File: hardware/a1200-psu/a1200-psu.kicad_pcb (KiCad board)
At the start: 2 copper layers, 147 x 76 mm, 61 parts, among them J1 220V, J2 Conn_01x05, Q1 P2N60, U1 UC3844_DIP8, U2 PC817, U3 TL431D

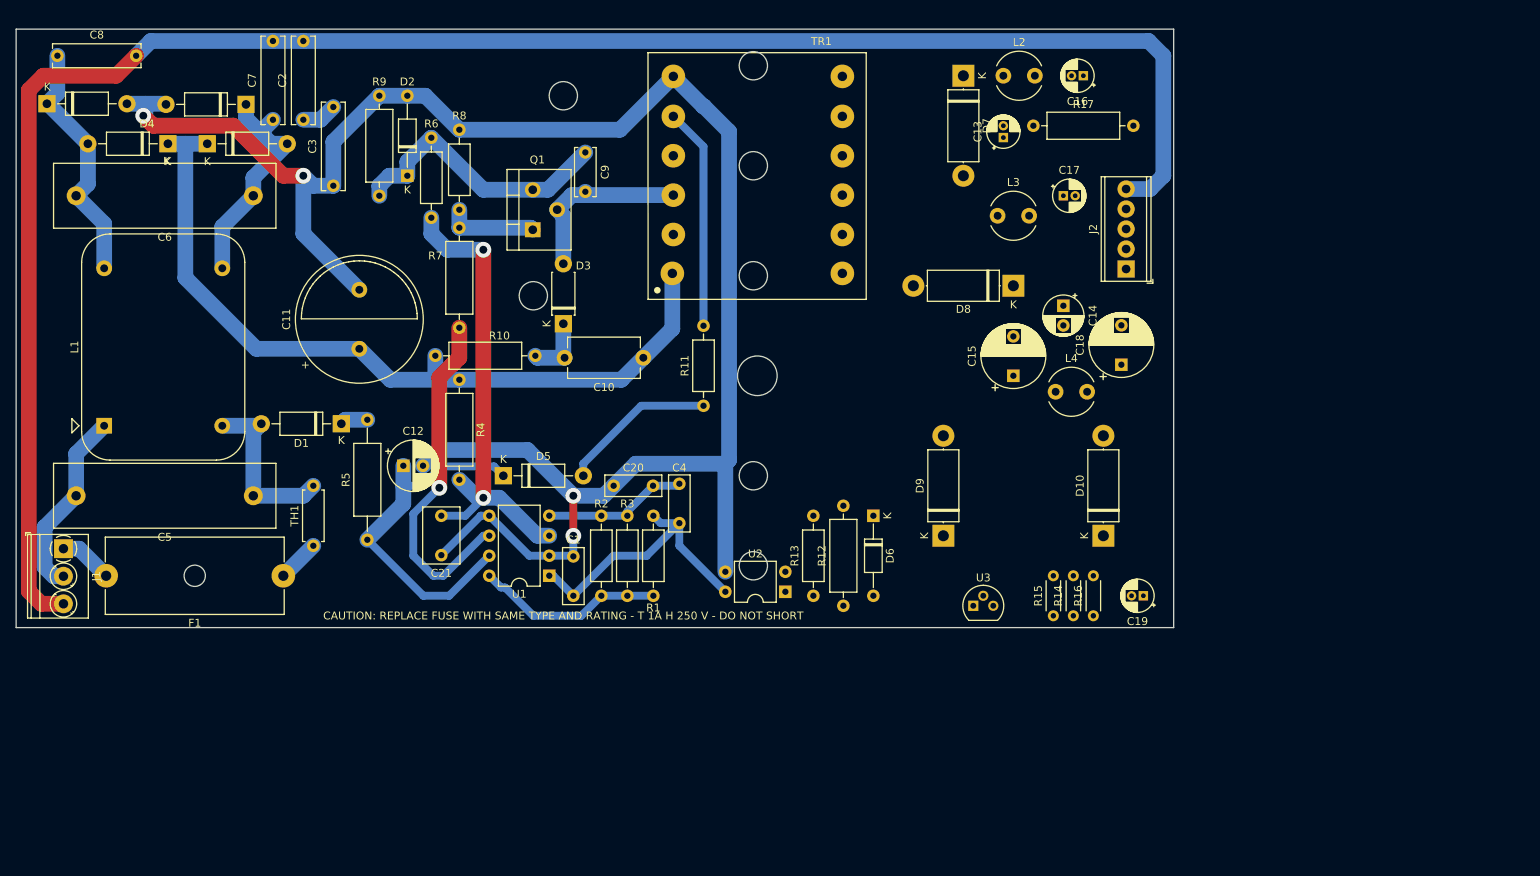
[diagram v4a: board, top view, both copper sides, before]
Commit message: Fixed ERC/DRC errors
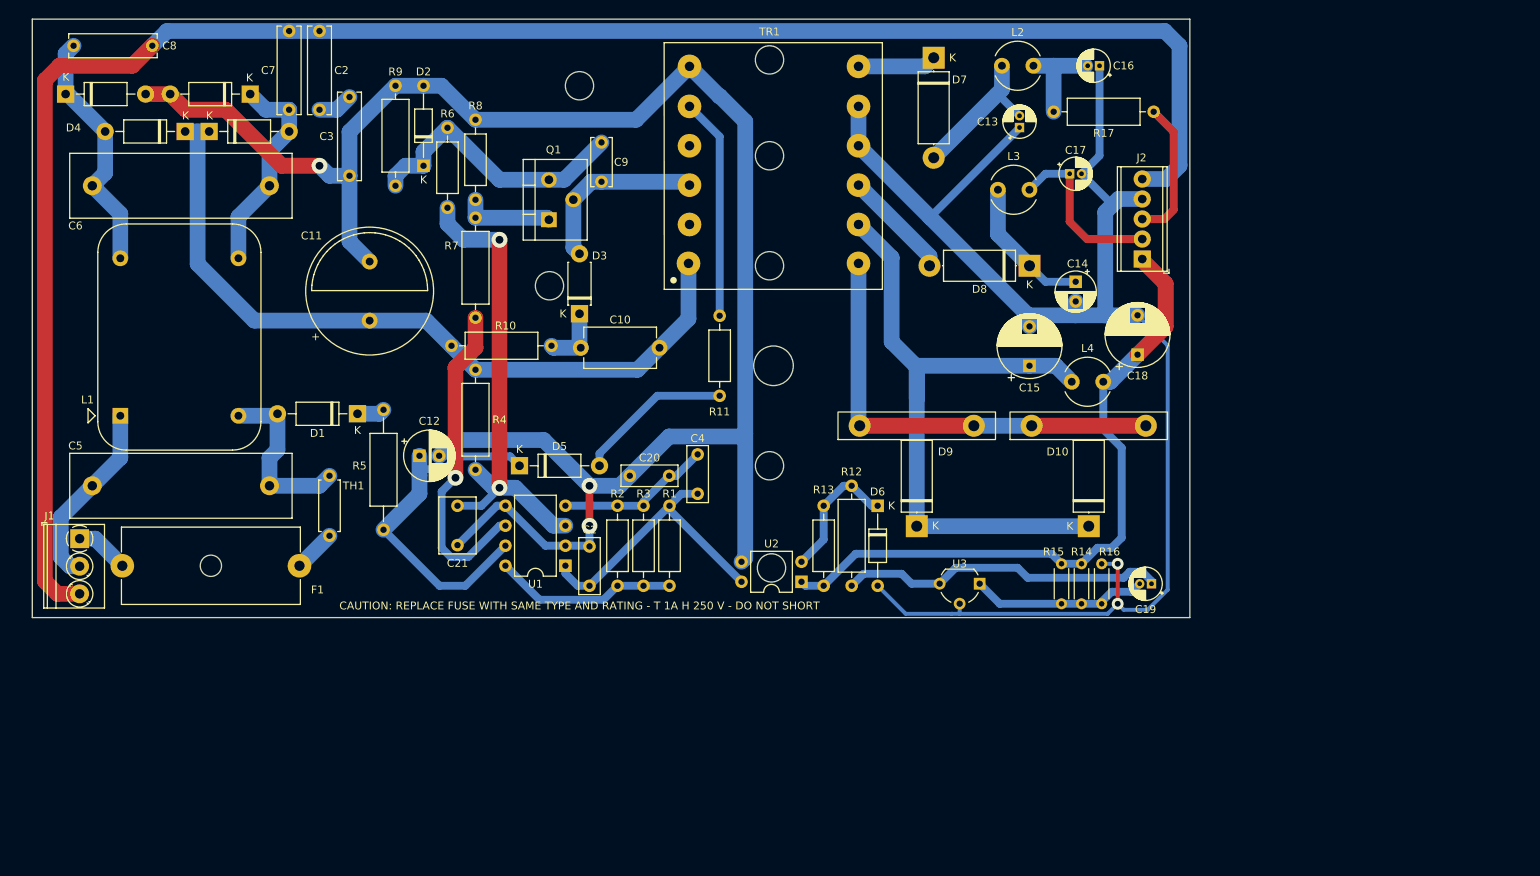
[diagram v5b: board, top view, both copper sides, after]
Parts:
- D10, D9: footprint Diode_THT:D_5W_P12.70mm_Horizontal -> Amiga 1200:Diode_Heatsink
- D6: value BZX55 -> ?
- J1: value 220V -> AC-In
- J2: value Conn_01x05 -> DC-Out
- R14: value 200k -> ?
- R15, R16: value 33k -> ?
- R17: value ? -> 330R
- U3: footprint Package_TO_SOT_THT:TO-92 -> Package_TO_SOT_THT:TO-92_Wide
- moved R17 15.4 mm to (172.7, 33.8), turned to 180 degrees
- moved R12 15.3 mm to (134.4, 81.3), turned to -90 degrees
- moved R13 11.5 mm to (130.8, 83.8), turned to -90 degrees
- moved R16 6.69 mm to (166.1, 91.2), turned to -90 degrees
- moved D7 4.41 mm to (144.8, 26.9)
- moved C4 4.40 mm to (114.8, 82.3)
- moved C11 3.81 mm to (73.2, 60.3)
- moved D9 3.59 mm to (142.7, 86.4)
- moved C14 3.43 mm to (162.8, 55.4)
- moved L3 3.30 mm to (153.0, 43.7)
- moved D8 3.27 mm to (157.0, 53.3)
- moved U3 2.92 mm to (150.6, 93.7), turned to 180 degrees
- moved C17 2.91 mm to (162.1, 41.7)
- moved C15 2.41 mm to (157.0, 66.0)
- moved C21 2.41 mm to (84.3, 83.8)
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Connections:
- net Net-(D10-Pad2) renamed /TR_5V
- C16 pad 2: -12V -> Net-(L2-Pad2)
- C19 pad 2: Net-(C19-Pad2) -> Net-(R14-Pad1)
- J2 pad 1: -12V -> +5V
- J2 pad 3: +5V -> -12V
- L2 pad 2: -12V -> Net-(L2-Pad2)
- R14 pad 1: GND -> Net-(R14-Pad1)
- R14 pad 2: Net-(C19-Pad2) -> +5V
- R15 pad 1: Net-(C19-Pad2) -> Net-(R14-Pad1)
- R16 pad 2: Net-(C19-Pad2) -> Net-(R14-Pad1)
- R17 pad 2: -12V -> Net-(L2-Pad2)
- U3 pad 1: Net-(C19-Pad2) -> Net-(R14-Pad1)
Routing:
- net GND: track 0.00 -> 192.5 mm, vias 0 -> 2
- net Net-(D10-Pad1): track 0.00 -> 87.9 mm
- net +5V: track 0.00 -> 85.9 mm
- net /TR_5V: track 0.00 -> 57.0 mm
- net Net-(R12-Pad2): track 0.00 -> 41.7 mm
- net Net-(R14-Pad1): track 0.00 -> 22.6 mm
- net +12V: track 0.00 -> 22.2 mm
- net Net-(D7-Pad2): track 0.00 -> 19.3 mm
- net Net-(D8-Pad1): track 0.00 -> 18.0 mm
- net -12V: track 0.00 -> 18.0 mm
- net Net-(D6-Pad1): track 0.00 -> 17.2 mm
- net Net-(D8-Pad2): track 0.00 -> 14.0 mm
- net Net-(L2-Pad2): track 0.00 -> 12.4 mm
- net Net-(D7-Pad1): track 0.00 -> 10.00 mm
- net GNDD: track 245.8 -> 237.4 mm, vias 4 -> 3
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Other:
- outline, holes or cut-outs redrawn
- board text removed: "!! WIP !!"

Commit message: Exported PNGs for 1F/1C
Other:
- board text added: "Amiga 1200 PSU Replica"
- board text added: "Board: 30501-001 A P-No: 391029-02 Rating: UK 220-240 V 300 mA"
- board text added: "Nick Bolton"
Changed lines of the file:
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@@
   (title_block
     (title "Amiga A1200 PSU UK 391029-02")
-    (date "2023-02-09")
-    (rev "1B")
+    (date "2023-02-11")
+    (rev "1C")
     (company "Nick Bolton")
   )
@@
       (effects (font (size 1 1) (thickness 0.15)))
     )
-    (fp_text value "821k" (at 4.826 -3.81) (layer "F.Fab")
+    (fp_text value "821k" (at 4.318 0 90) (layer "F.Fab")
       (effects (font (size 1 1) (thickness 0.15)))
     )
-    (fp_text user "${REFERENCE}" (at 6.35 0 180) (layer "F.Fab")
+    (fp_text user "${REFERENCE}" (at 8.128 0 180) (layer "F.Fab")
       (effects (font (size 1 1) (thickness 0.15)))
     )
@@
       (effects (font (size 1 1) (thickness 0.15)))
     )
-    (fp_text value "10nF" (at 2.5 2.5 90) (layer "F.Fab")
+    (fp_text value "10nF" (at 2.587 -0.635 90) (layer "F.Fab")
       (effects (font (size 1 1) (thickness 0.15)))
     )
-    (fp_text user "${REFERENCE}" (at 2.5 0 90) (layer "F.Fab")
+    (fp_text user "${REFERENCE}" (at 2.5 0.508 90) (layer "F.Fab")
       (effects (font (size 1 1) (thickness 0.15)))
     )
@@
     (property "Sheetname" "")
     (attr through_hole)
-    (fp_text reference "L1" (at 2.032 -4.172 180) (layer "F.SilkS")
+    (fp_text reference "L1" (at 11.43 18.942 180) (layer "F.SilkS")
       (effects (font (size 1 1) (thickness 0.15)))
     )
-    (fp_text value "47mH" (at 3.302 -5.442 180) (layer "F.Fab")
+    (fp_text value "47mH" (at 9.779 20.085 180) (layer "F.Fab")
       (effects (font (size 1 1) (thickness 0.15)))
     )
@@
   (gr_rect (start 31.242 22.86) (end 123.19 97.282) (layer "User.9") (width 0.15) (fill none))
   (gr_rect (start 125.222 97.282) (end 176.53 22.86) (layer "User.9") (width 0.15) (fill none))
+  (gr_text "Nick Bolton" (at 88.773 27.94) (layer "F.SilkS")
+    (effects (font (size 1.5 1.5) (thickness 0.2)))
+  )
   (gr_text "CAUTION: REPLACE FUSE WITH SAME TYPE AND RATING - T 1A H 250 V - DO NOT SHORT" (at 99.822 96.52) (layer "F.SilkS")
     (effects (font (size 1 1) (thickness 0.25)))
@@
     (effects (font (size 1 1) (thickness 0.15)))
   )
+  (gr_text "Board: 30501-001 A\nP-No: 391029-02\nRating: UK 220-240 V 300 mA" (at 34.163 62.103 90) (layer "F.SilkS")
+    (effects (font (size 1 1) (thickness 0.15)))
+  )
+  (gr_text "Amiga 1200 PSU Replica" (at 90.297 25.146) (layer "F.SilkS")
+    (effects (font (size 2 2) (thickness 0.3)))
+  )
   (gr_text "AC/DC line voltage" (at 43.18 20.32) (layer "Cmts.User")

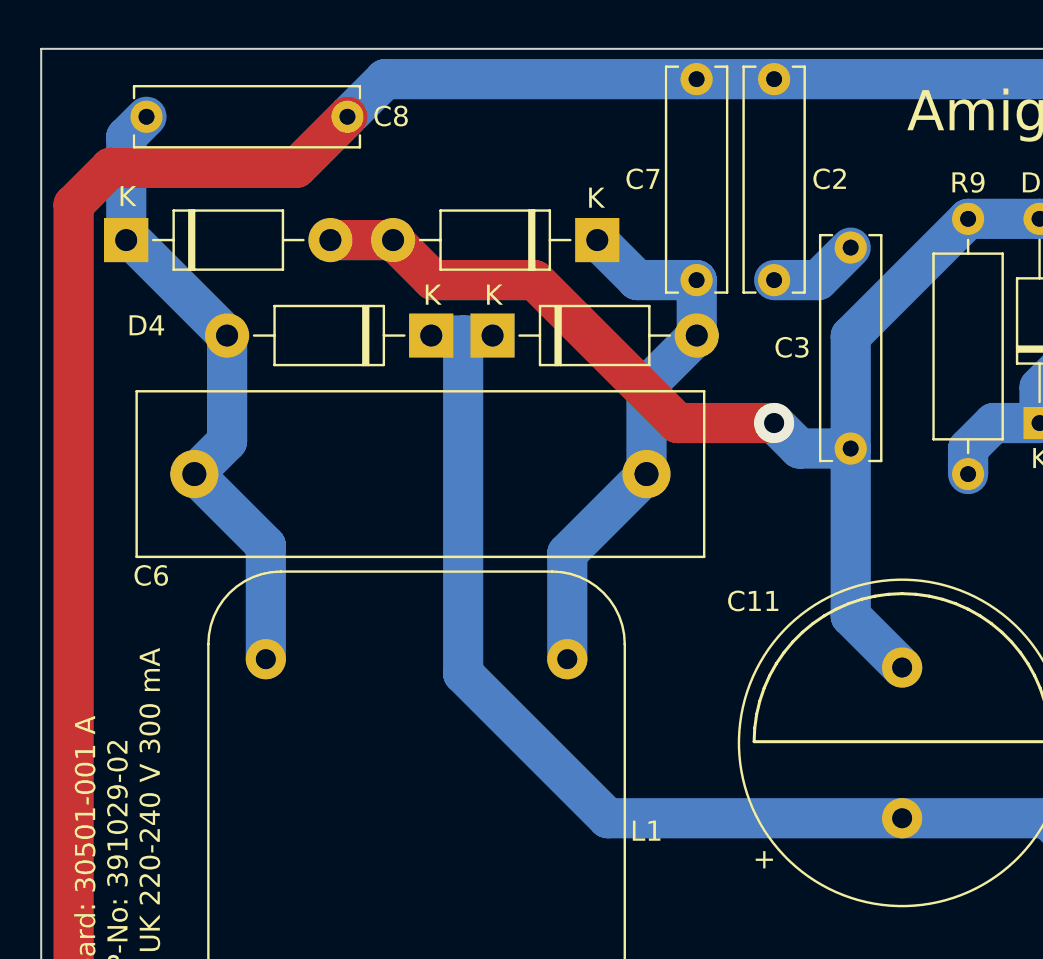
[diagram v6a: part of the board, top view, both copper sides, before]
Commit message: Started on filled zones
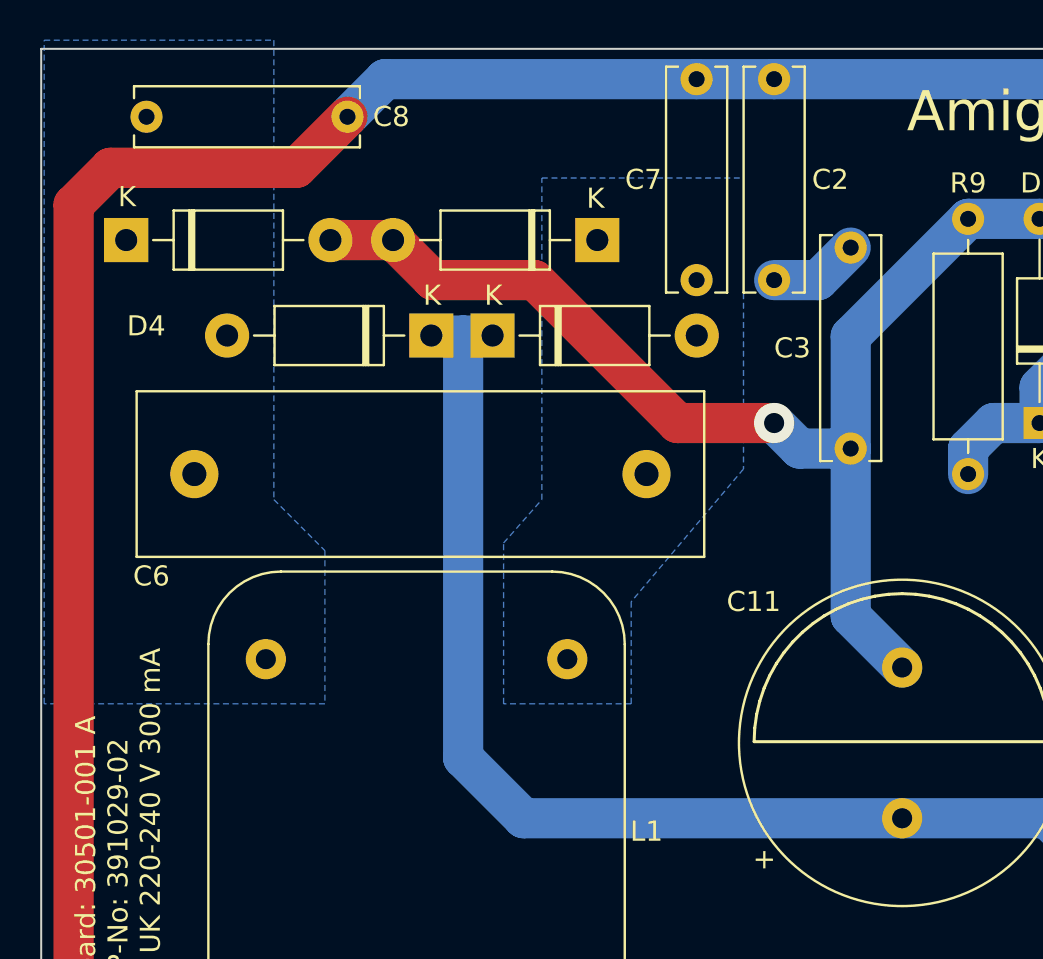
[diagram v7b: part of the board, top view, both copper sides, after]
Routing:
- net Net-(C6-Pad2): track 31.8 -> 0.00 mm
- net Net-(C6-Pad1): track 27.3 -> 0.00 mm
- net Net-(C10-Pad1): track 97.5 -> 99.9 mm
- added copper zone on B.Cu, net Net-(C6-Pad1)
- added copper zone on B.Cu, net Net-(C6-Pad2)
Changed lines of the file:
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@@
   (segment (start 49.742 36.286) (end 52.792 36.286) (width 2) (layer "B.Cu") (net 6))
   (segment (start 109.982 63.754) (end 107.188 66.548) (width 2) (layer "B.Cu") (net 6))
+  (segment (start 51.328 57.297) (end 51.328 36.286) (width 2) (layer "B.Cu") (net 6))
   (segment (start 83.566 63.5) (end 86.614 66.548) (width 2) (layer "B.Cu") (net 6))
-  (segment (start 58.527172 60.305172) (end 51.328 53.106) (width 2) (layer "B.Cu") (net 6))
-  (segment (start 51.328 53.106) (end 51.328 36.286) (width 2) (layer "B.Cu") (net 6))
+  (segment (start 54.336172 60.305172) (end 51.328 57.297) (width 2) (layer "B.Cu") (net 6))
+  (segment (start 73.172 60.305172) (end 54.336172 60.305172) (width 2) (layer "B.Cu") (net 6))
   (segment (start 107.188 66.548) (end 86.614 66.548) (width 2) (layer "B.Cu") (net 6))
   (segment (start 113.665 53.039) (end 113.665 60.071) (width 2) (layer "B.Cu") (net 6))
   (segment (start 80.371172 60.305172) (end 83.566 63.5) (width 2) (layer "B.Cu") (net 6))
-  (segment (start 73.172 60.305172) (end 58.527172 60.305172) (width 2) (layer "B.Cu") (net 6))
   (segment (start 113.665 60.071) (end 109.982 63.754) (width 2) (layer "B.Cu") (net 6))
   (segment (start 73.172 60.305172) (end 80.371172 60.305172) (width 2) (layer "B.Cu") (net 6))
@@
   (segment (start 60.452 81.28) (end 60.452 77.744) (width 2) (layer "B.Cu") (net 18))
   (segment (start 66.802 81.28) (end 68.072 80.01) (width 2) (layer "B.Cu") (net 18))
-  (segment (start 59.994 33.528) (end 58.002 31.536) (width 2) (layer "B.Cu") (net 19))
-  (segment (start 60.452 38.786) (end 62.952 36.286) (width 2) (layer "B.Cu") (net 19))
-  (segment (start 56.51 47.122) (end 60.452 43.18) (width 2) (layer "B.Cu") (net 19))
-  (segment (start 62.952 33.536) (end 62.944 33.528) (width 2) (layer "B.Cu") (net 19))
-  (segment (start 62.944 33.528) (end 59.994 33.528) (width 2) (layer "B.Cu") (net 19))
-  (segment (start 56.51 52.39) (end 56.51 47.122) (width 2) (layer "B.Cu") (net 19))
-  (segment (start 60.452 43.18) (end 60.452 38.786) (width 2) (layer "B.Cu") (net 19))
-  (segment (start 62.952 36.286) (end 62.952 33.536) (width 2) (layer "B.Cu") (net 19))
   (segment (start 41.51 77.722) (end 41.51 72.39) (width 2) (layer "B.Cu") (net 20))
   (segment (start 33.9415 85.2905) (end 37.952 81.28) (width 2) (layer "B.Cu") (net 20))
@@
   (segment (start 35.111 91.499) (end 33.9415 90.3295) (width 2) (layer "B.Cu") (net 20))
   (segment (start 33.9415 90.3295) (end 33.9415 85.2905) (width 2) (layer "B.Cu") (net 20))
-  (segment (start 35.572 25.4) (end 34.564 26.408) (width 2) (layer "B.Cu") (net 21))
-  (segment (start 34.832 31.536) (end 39.582 36.286) (width 2) (layer "B.Cu") (net 21))
-  (segment (start 34.562 31.536) (end 34.832 31.536) (width 2) (layer "B.Cu") (net 21))
-  (segment (start 39.582 41.55) (end 37.952 43.18) (width 2) (layer "B.Cu") (net 21))
-  (segment (start 34.564 26.408) (end 34.564 31.534) (width 2) (layer "B.Cu") (net 21))
-  (segment (start 39.582 36.286) (end 39.582 41.55) (width 2) (layer "B.Cu") (net 21))
-  (segment (start 41.51 46.738) (end 37.952 43.18) (width 2) (layer "B.Cu") (net 21))
-  (segment (start 41.51 52.39) (end 41.51 46.738) (width 2) (layer "B.Cu") (net 21))
   (segment (start 134.386 81.28) (end 133.37 81.28) (width 1) (layer "B.Cu") (net 22))
   (segment (start 130.83 83.82) (end 130.83 88.118) (width 1) (layer "B.Cu") (net 22))
@@
   (segment (start 36.3415 87.999) (end 38.321 87.999) (width 2) (layer "B.Cu") (net 39))
   (segment (start 38.321 87.999) (end 41.762 91.44) (width 2) (layer "B.Cu") (net 39))
+  (zone (net 19) (net_name "Net-(C6-Pad1)") (layer "B.Cu") (hatch edge 0.508)
+    (connect_pads (clearance 0.508))
+    (min_thickness 0.254) (filled_areas_thickness no)
+    (fill yes (thermal_gap 0.508) (thermal_bridge_width 0.508) (smoothing fillet) (radius 1))
+    (polygon
+      (pts
+        (xy 65.278 42.926)
+        (xy 59.69 49.53)
+        (xy 59.69 54.61)
+        (xy 53.34 54.61)
+        (xy 53.34 46.609)
+        (xy 55.245 44.45)
+        (xy 55.245 28.448)
+        (xy 65.278 28.448)
+      )
+    )
+  )
+  (zone (net 21) (net_name "Net-(C6-Pad2)") (layer "B.Cu") (hatch edge 0.508)
+    (connect_pads (clearance 0.508))
+    (min_thickness 0.254) (filled_areas_thickness no)
+    (fill yes (thermal_gap 0.508) (thermal_bridge_width 0.508) (smoothing fillet) (radius 1))
+    (polygon
+      (pts
+        (xy 41.91 44.45)
+        (xy 44.45 46.99)
+        (xy 44.45 54.61)
+        (xy 30.48 54.61)
+        (xy 30.48 21.59)
+        (xy 41.91 21.59)
+      )
+    )
+  )
   (group "" (id b4997917-b90b-4111-8527-b943698119cb)
     (members
